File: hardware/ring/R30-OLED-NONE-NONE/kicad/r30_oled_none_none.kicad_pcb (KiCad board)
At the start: 2 copper layers, 42 x 18 mm, 32 parts, among them J1 USB4215-class 16P TH stakes, Q1 SI2301 P-FET, Q2 2N7002 gate driver, SW1 5mm 200gf dome, U1 ESP32-C3-MINI-1-N4, U2 PAW3204DB-TJ3L, U3 TP4054, U4 RT9080-33GJ5

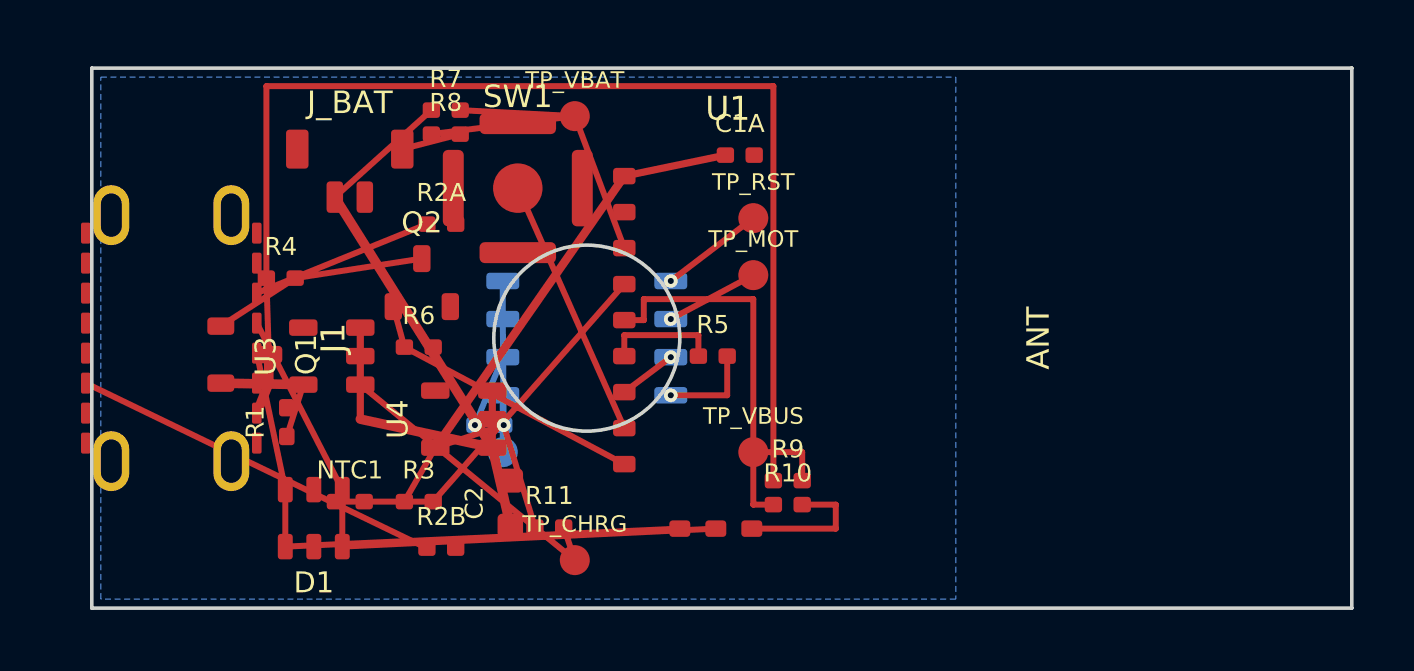
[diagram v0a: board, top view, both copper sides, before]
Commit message: fix(r30): move charge bias off usb cc row
Sensing mechanism: PAW3204 optical surface tracking.

Form factor and angle: R30 30-degree ring, OLED/NONE/NONE active lane.

Intended use: accessibility-first BLE HID pointing first-board validation.

BOM estimate: active R30 prototype remains about $5.30-$9.45, target about $9.
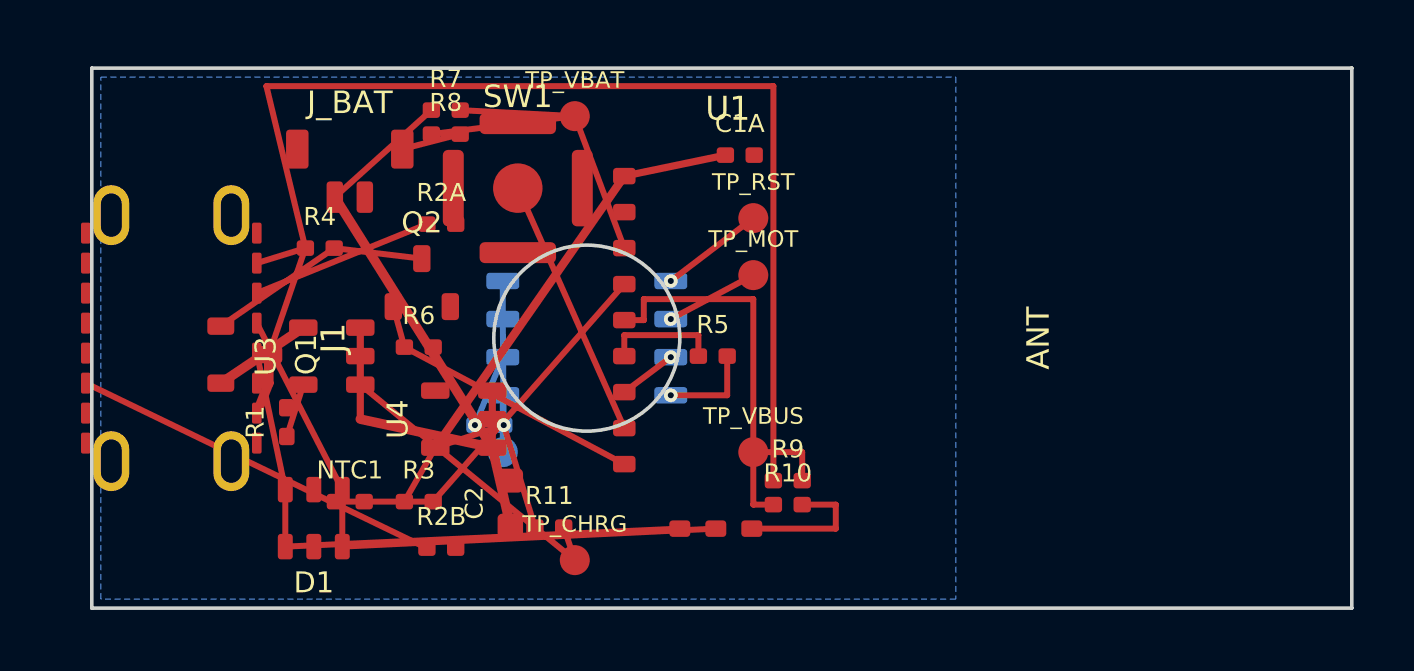
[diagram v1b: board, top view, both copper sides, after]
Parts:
- moved R4 1.64 mm to (107.6, 97.0)
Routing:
- net VBUS_5V: track 41.0 -> 43.1 mm
- net VBUS_CHG_SW: track 2.75 -> 3.31 mm
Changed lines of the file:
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@@
   (footprint "Resistor_SMD:R_0402_1005Metric"
     (layer "F.Cu")
-    (at 106.300 98.000 0)
+    (at 107.600 97.000 0)
     (property "Reference" "R4" (at 0 -1.05 0) (layer "F.SilkS") (effects (font (size 0.6 0.6) (thickness 0.09))))
     (property "Value" "100k" (at 0 1.05 0) (layer "F.Fab") (effects (font (size 0.55 0.55) (thickness 0.08))))
@@
   (segment (start 105.500 102.500) (end 105.900 101.500) (width 0.32) (layer "F.Cu") (net 2))
   (segment (start 105.900 101.500) (end 105.900 100.550) (width 0.32) (layer "F.Cu") (net 2))
-  (segment (start 105.820 98.000) (end 105.900 100.550) (width 0.20) (layer "F.Cu") (net 2))
-  (segment (start 104.300 101.500) (end 107.050 101.550) (width 0.32) (layer "F.Cu") (net 3))
+  (segment (start 105.500 97.500) (end 107.120 97.000) (width 0.20) (layer "F.Cu") (net 2))
+  (segment (start 107.120 97.000) (end 105.900 100.550) (width 0.20) (layer "F.Cu") (net 2))
+  (segment (start 104.300 101.500) (end 107.050 99.650) (width 0.32) (layer "F.Cu") (net 3))
   (segment (start 108.950 99.650) (end 108.950 102.700) (width 0.24) (layer "F.Cu") (net 4))
   (segment (start 108.950 102.700) (end 113.350 103.650) (width 0.32) (layer "F.Cu") (net 4))
@@
   (segment (start 112.770 102.900) (end 113.700 100.635) (width 0.20) (layer "B.Cu") (net 1))
   (segment (start 107.050 101.550) (end 106.500 103.280) (width 0.20) (layer "F.Cu") (net 6))
-  (segment (start 104.300 99.600) (end 106.780 98.000) (width 0.20) (layer "F.Cu") (net 7))
-  (segment (start 106.780 98.000) (end 111.000 97.350) (width 0.20) (layer "F.Cu") (net 7))
+  (segment (start 104.300 99.600) (end 108.080 97.000) (width 0.20) (layer "F.Cu") (net 7))
+  (segment (start 108.080 97.000) (end 111.000 97.350) (width 0.20) (layer "F.Cu") (net 7))
   (segment (start 110.050 98.950) (end 110.420 100.300) (width 0.20) (layer "F.Cu") (net 8))
   (segment (start 110.420 100.300) (end 117.750 104.200) (width 0.20) (layer "F.Cu") (net 8))
   (segment (start 111.320 92.400) (end 108.100 95.300) (width 0.20) (layer "F.Cu") (net 4))
   (segment (start 112.280 93.200) (end 110.350 93.700) (width 0.20) (layer "F.Cu") (net 1))
-  (segment (start 105.820 98.000) (end 105.820 91.600) (width 0.20) (layer "F.Cu") (net 2))
+  (segment (start 107.120 97.000) (end 105.820 91.600) (width 0.20) (layer "F.Cu") (net 2))
   (segment (start 105.820 91.600) (end 122.720 91.600) (width 0.20) (layer "F.Cu") (net 2))
   (segment (start 122.720 91.600) (end 122.720 104.750) (width 0.20) (layer "F.Cu") (net 2))

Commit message: fix(r30): move charger switch off usb data row
Sensing mechanism: PAW3204 optical surface tracking.

Form factor and angle: R30 30-degree ring, OLED/NONE/NONE active lane.

Intended use: accessibility-first BLE HID pointing first-board validation.

BOM estimate: active R30 prototype remains about $5.30-$9.45, target about $9.
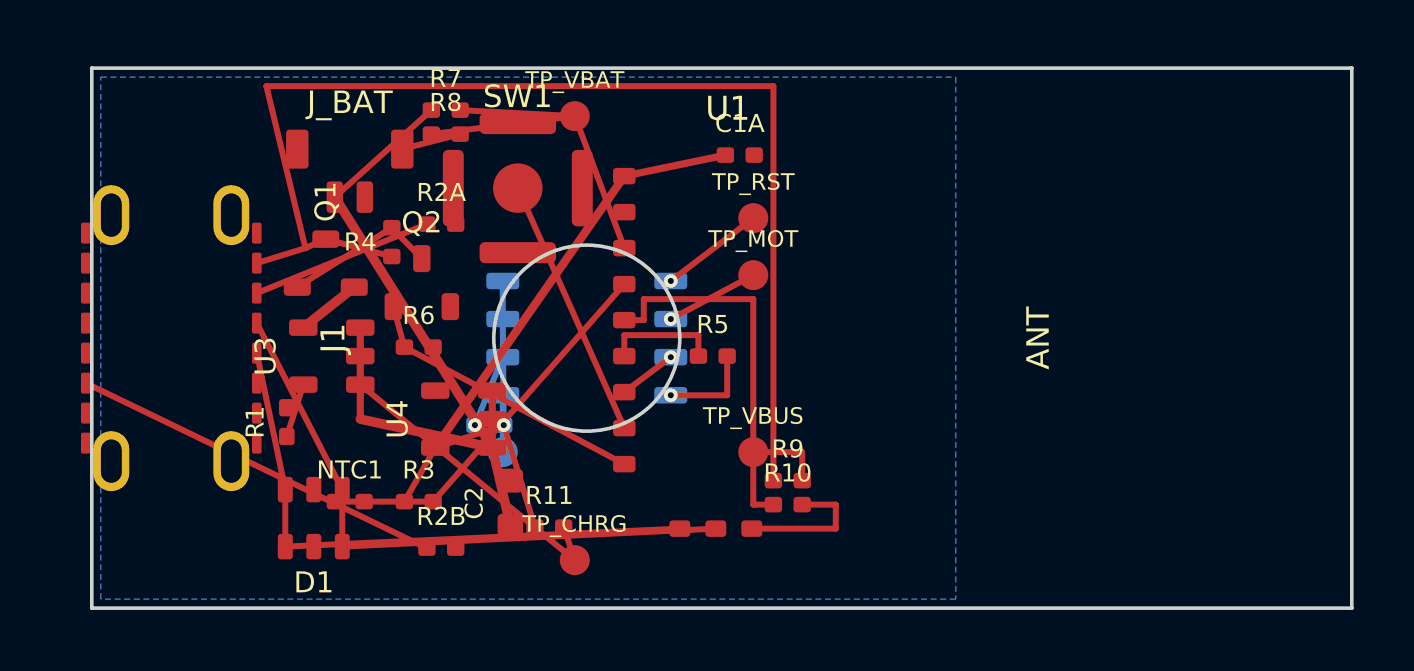
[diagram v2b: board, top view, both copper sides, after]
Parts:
- moved Q1 4.07 mm to (107.8, 97.5), turned to 0 degrees
- moved R4 2.41 mm to (110.0, 96.8), turned to 90 degrees
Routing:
- net VBUS_5V: track 43.1 -> 40.3 mm
- net CHARGE_GATE: track 7.53 -> 5.16 mm
- net VBUS_CHG_SW: track 3.31 -> 2.17 mm
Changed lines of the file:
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@@
   (footprint "Package_TO_SOT_SMD:SOT-23"
     (layer "F.Cu")
-    (at 105.100 100.550 270)
+    (at 107.800 97.500 0)
     (property "Reference" "Q1" (at 0 -2.05 270) (layer "F.SilkS") (effects (font (size 0.7 0.7) (thickness 0.1))))
     (property "Value" "SI2301 P-FET" (at 0 2.05 270) (layer "F.Fab") (effects (font (size 0.7 0.7) (thickness 0.1))))
@@
   (footprint "Resistor_SMD:R_0402_1005Metric"
     (layer "F.Cu")
-    (at 107.600 97.000 0)
+    (at 110.000 96.800 90)
     (property "Reference" "R4" (at 0 -1.05 0) (layer "F.SilkS") (effects (font (size 0.6 0.6) (thickness 0.09))))
     (property "Value" "100k" (at 0 1.05 0) (layer "F.Fab") (effects (font (size 0.55 0.55) (thickness 0.08))))
@@
     (pad "1" smd circle (at 0 0) (size 1.00 1.00) (layers "B.Cu" "B.Mask") (net 23 "SENSOR_LED_KIT") (pinfunction "1") (pintype "passive"))
   )
-  (segment (start 105.500 102.500) (end 105.900 101.500) (width 0.32) (layer "F.Cu") (net 2))
-  (segment (start 105.900 101.500) (end 105.900 100.550) (width 0.32) (layer "F.Cu") (net 2))
   (segment (start 105.500 97.500) (end 107.120 97.000) (width 0.20) (layer "F.Cu") (net 2))
-  (segment (start 107.120 97.000) (end 105.900 100.550) (width 0.20) (layer "F.Cu") (net 2))
-  (segment (start 104.300 101.500) (end 107.050 99.650) (width 0.32) (layer "F.Cu") (net 3))
+  (segment (start 107.120 97.000) (end 107.800 96.700) (width 0.20) (layer "F.Cu") (net 2))
+  (segment (start 107.800 96.700) (end 110.000 97.280) (width 0.20) (layer "F.Cu") (net 2))
+  (segment (start 108.750 98.300) (end 107.050 99.650) (width 0.32) (layer "F.Cu") (net 3))
   (segment (start 108.950 99.650) (end 108.950 102.700) (width 0.24) (layer "F.Cu") (net 4))
   (segment (start 108.950 102.700) (end 113.350 103.650) (width 0.32) (layer "F.Cu") (net 4))
@@
   (segment (start 112.770 102.900) (end 113.700 100.635) (width 0.20) (layer "B.Cu") (net 1))
   (segment (start 107.050 101.550) (end 106.500 103.280) (width 0.20) (layer "F.Cu") (net 6))
-  (segment (start 104.300 99.600) (end 108.080 97.000) (width 0.20) (layer "F.Cu") (net 7))
-  (segment (start 108.080 97.000) (end 111.000 97.350) (width 0.20) (layer "F.Cu") (net 7))
+  (segment (start 106.850 98.300) (end 110.000 96.320) (width 0.20) (layer "F.Cu") (net 7))
+  (segment (start 110.000 96.320) (end 111.000 97.350) (width 0.20) (layer "F.Cu") (net 7))
   (segment (start 110.050 98.950) (end 110.420 100.300) (width 0.20) (layer "F.Cu") (net 8))
   (segment (start 110.420 100.300) (end 117.750 104.200) (width 0.20) (layer "F.Cu") (net 8))

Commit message: fix(r30): separate usb data lanes
Sensing mechanism: PAW3204 optical surface tracking.

Form factor and angle: R30 30-degree ring, OLED/NONE/NONE active lane.

Intended use: accessibility-first BLE HID pointing first-board validation.

BOM estimate: active R30 prototype remains about $5.30-$9.45, target about $9.
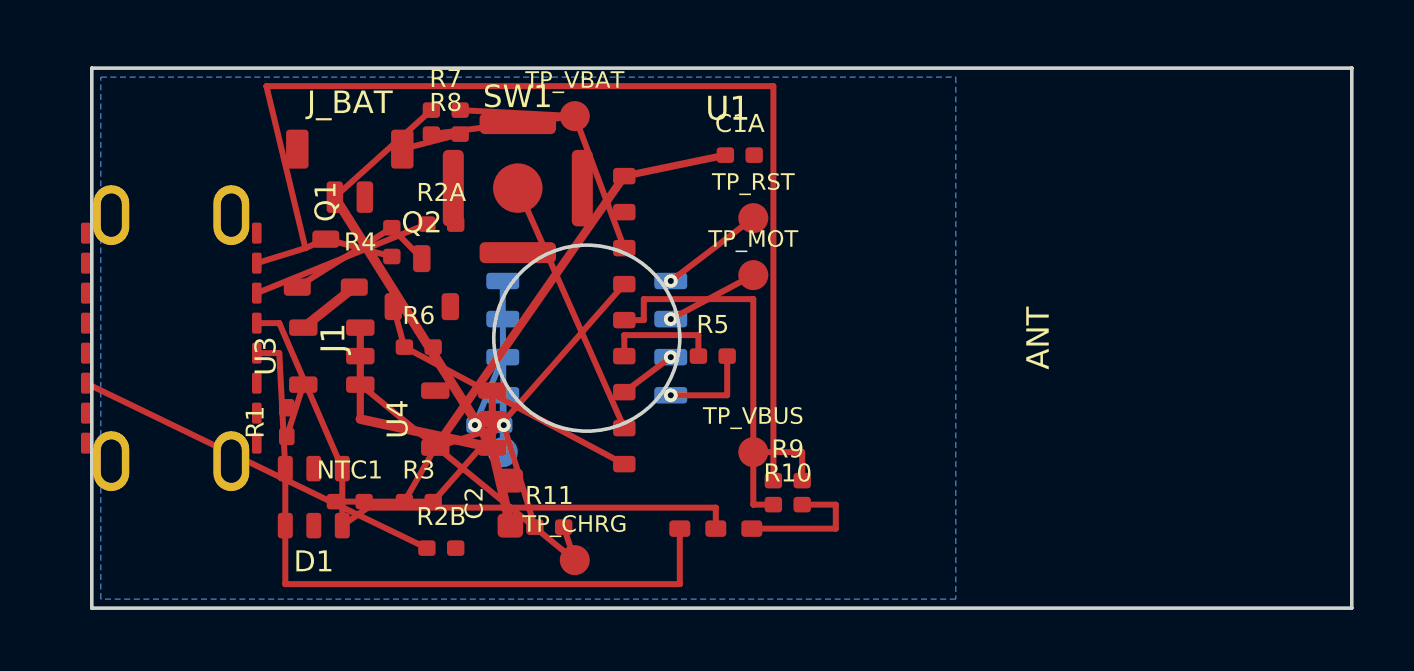
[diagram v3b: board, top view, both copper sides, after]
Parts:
- moved D1 0.70 mm to (107.4, 105.3)
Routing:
- net USB_D-: track 19.7 -> 23.5 mm
- net USB_D+: track 20.6 -> 21.3 mm
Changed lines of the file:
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@@
   (footprint "Package_TO_SOT_SMD:SOT-23-6"
     (layer "F.Cu")
-    (at 107.400 106.000 180)
+    (at 107.400 105.300 180)
     (property "Reference" "D1" (at 0 -2.15 180) (layer "F.SilkS") (effects (font (size 0.7 0.7) (thickness 0.1))))
     (property "Value" "USBLC6-2SC6-class" (at 0 2.15 180) (layer "F.Fab") (effects (font (size 0.7 0.7) (thickness 0.1))))
@@
   (segment (start 119.300 98.095) (end 122.050 96.000) (width 0.20) (layer "F.Cu") (net 14))
   (segment (start 117.750 103.000) (end 114.200 95.000) (width 0.20) (layer "F.Cu") (net 15))
-  (segment (start 105.500 99.500) (end 108.350 105.050) (width 0.20) (layer "F.Cu") (net 16))
-  (segment (start 108.350 106.950) (end 120.800 106.350) (width 0.20) (layer "F.Cu") (net 16))
-  (segment (start 108.350 105.050) (end 108.350 106.950) (width 0.20) (layer "F.Cu") (net 16))
-  (segment (start 105.500 100.500) (end 106.450 105.050) (width 0.20) (layer "F.Cu") (net 17))
-  (segment (start 106.450 106.950) (end 119.600 106.350) (width 0.20) (layer "F.Cu") (net 17))
-  (segment (start 106.450 105.050) (end 106.450 106.950) (width 0.20) (layer "F.Cu") (net 17))
+  (segment (start 105.500 99.500) (end 106.250 99.500) (width 0.20) (layer "F.Cu") (net 16))
+  (segment (start 106.250 99.500) (end 108.350 104.350) (width 0.20) (layer "F.Cu") (net 16))
+  (segment (start 108.350 104.350) (end 108.350 106.250) (width 0.20) (layer "F.Cu") (net 16))
+  (segment (start 108.350 106.250) (end 109.200 105.650) (width 0.20) (layer "F.Cu") (net 16))
+  (segment (start 109.200 105.650) (end 120.800 105.650) (width 0.20) (layer "F.Cu") (net 16))
+  (segment (start 120.800 105.650) (end 120.800 106.350) (width 0.20) (layer "F.Cu") (net 16))
+  (segment (start 105.500 100.500) (end 106.250 100.500) (width 0.20) (layer "F.Cu") (net 17))
+  (segment (start 106.250 100.500) (end 106.450 104.350) (width 0.20) (layer "F.Cu") (net 17))
+  (segment (start 106.450 104.350) (end 106.450 106.250) (width 0.20) (layer "F.Cu") (net 17))
+  (segment (start 106.450 106.250) (end 106.450 108.200) (width 0.20) (layer "F.Cu") (net 17))
+  (segment (start 106.450 108.200) (end 119.600 108.200) (width 0.20) (layer "F.Cu") (net 17))
+  (segment (start 119.600 108.200) (end 119.600 106.350) (width 0.20) (layer "F.Cu") (net 17))
   (segment (start 105.500 98.500) (end 111.170 96.200) (width 0.20) (layer "F.Cu") (net 18))
   (segment (start 99.800 101.500) (end 111.170 107.000) (width 0.20) (layer "F.Cu") (net 19))

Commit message: fix(r30): contain usb service edge
Sensing mechanism: PAW3204 optical surface tracking.

Form factor and angle: R30 30-degree ring, OLED/NONE/NONE active lane; left USB-C service edge widened to the 43 x 18 mm board datum.

Intended use: accessibility-first BLE HID pointing first-board validation.

BOM estimate: active R30 prototype remains about .30-.45, target about ; outline and routing-only change adds no BOM line.
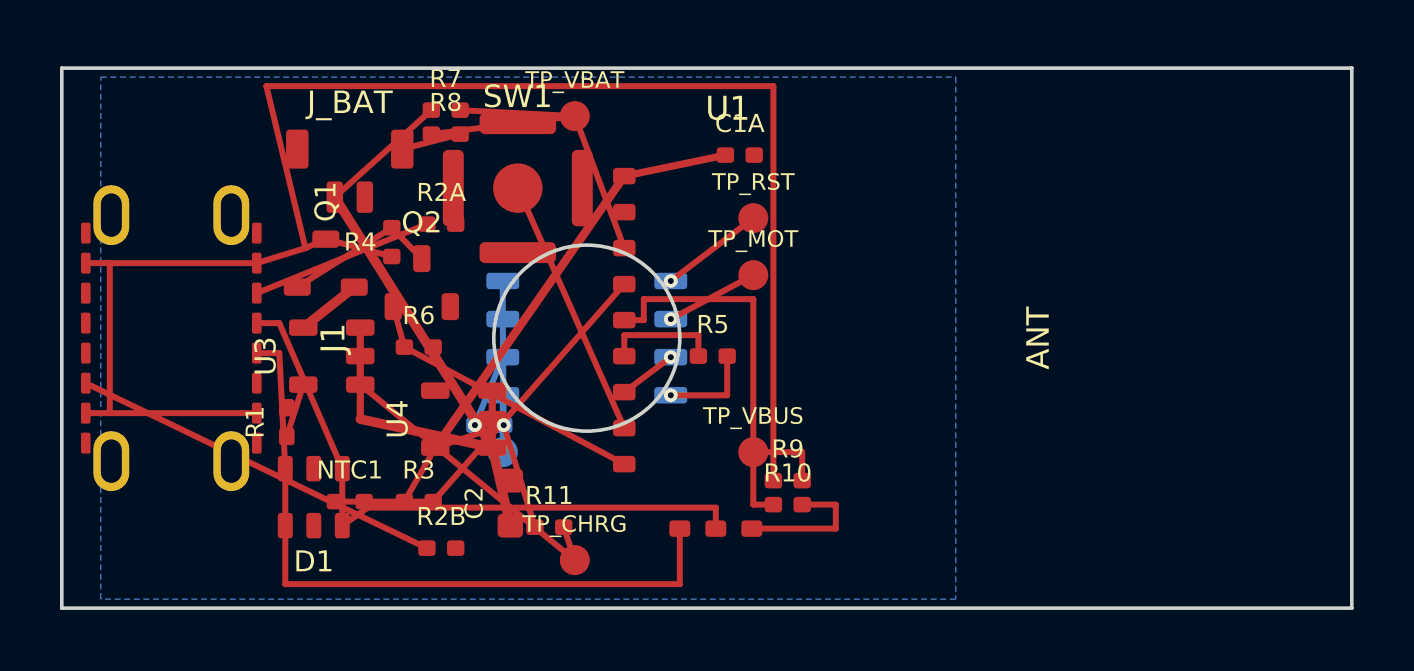
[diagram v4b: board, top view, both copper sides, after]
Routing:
- net VBUS_5V: track 40.3 -> 56.7 mm
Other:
- board size 42 x 18 mm -> 43 x 18 mm
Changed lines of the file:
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@@
   (net 23 "SENSOR_LED_KIT")
   (gr_rect
-    (start 100.000 91.000)
+    (start 99.000 91.000)
     (end 142.000 109.000)
     (stroke (width 0.12) (type solid))
@@
   )
   (gr_text "P0 is routed as a rigid validation board; shell fit remains red until measured."
-    (at 121.000 111.000 0)
+    (at 120.500 111.000 0)
     (layer "Cmts.User")
     (effects (font (size 0.85 0.85) (thickness 0.12)))
@@
   )
   (segment (start 105.500 97.500) (end 107.120 97.000) (width 0.20) (layer "F.Cu") (net 2))
+  (segment (start 99.800 97.500) (end 105.500 97.500) (width 0.20) (layer "F.Cu") (net 2))
+  (segment (start 99.800 102.500) (end 100.600 102.500) (width 0.20) (layer "F.Cu") (net 2))
+  (segment (start 100.600 102.500) (end 100.600 97.500) (width 0.20) (layer "F.Cu") (net 2))
+  (segment (start 100.600 102.500) (end 105.500 102.500) (width 0.20) (layer "F.Cu") (net 2))
   (segment (start 107.120 97.000) (end 107.800 96.700) (width 0.20) (layer "F.Cu") (net 2))
   (segment (start 107.800 96.700) (end 110.000 97.280) (width 0.20) (layer "F.Cu") (net 2))
